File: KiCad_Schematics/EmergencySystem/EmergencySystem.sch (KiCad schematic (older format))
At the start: 20 parts, among them SW1 E-Stop_Switch, SW2 ON/OFF_Switch, SW3 E-StopButton02, SW4 E-StopButton01, SW5 ON/OFF_Switch, U1 Feather_32u4_RFM95, U10 Adafruit_2200mAh_LiPo, U11 e-Boot_BuckConverter, U2 T3_EmergencyLight_RED, U3 T3_EmergencyLight_BLUE, U4 T3_EmergencyLight_AMBER, U5 Adafruit_2200mAh_LiPo, U6 OLED_I2C_Display, U7 Elegoo_4RelayModule, U8 e-Boot_BuckConverter, U9 Feather_32u4_RFM95

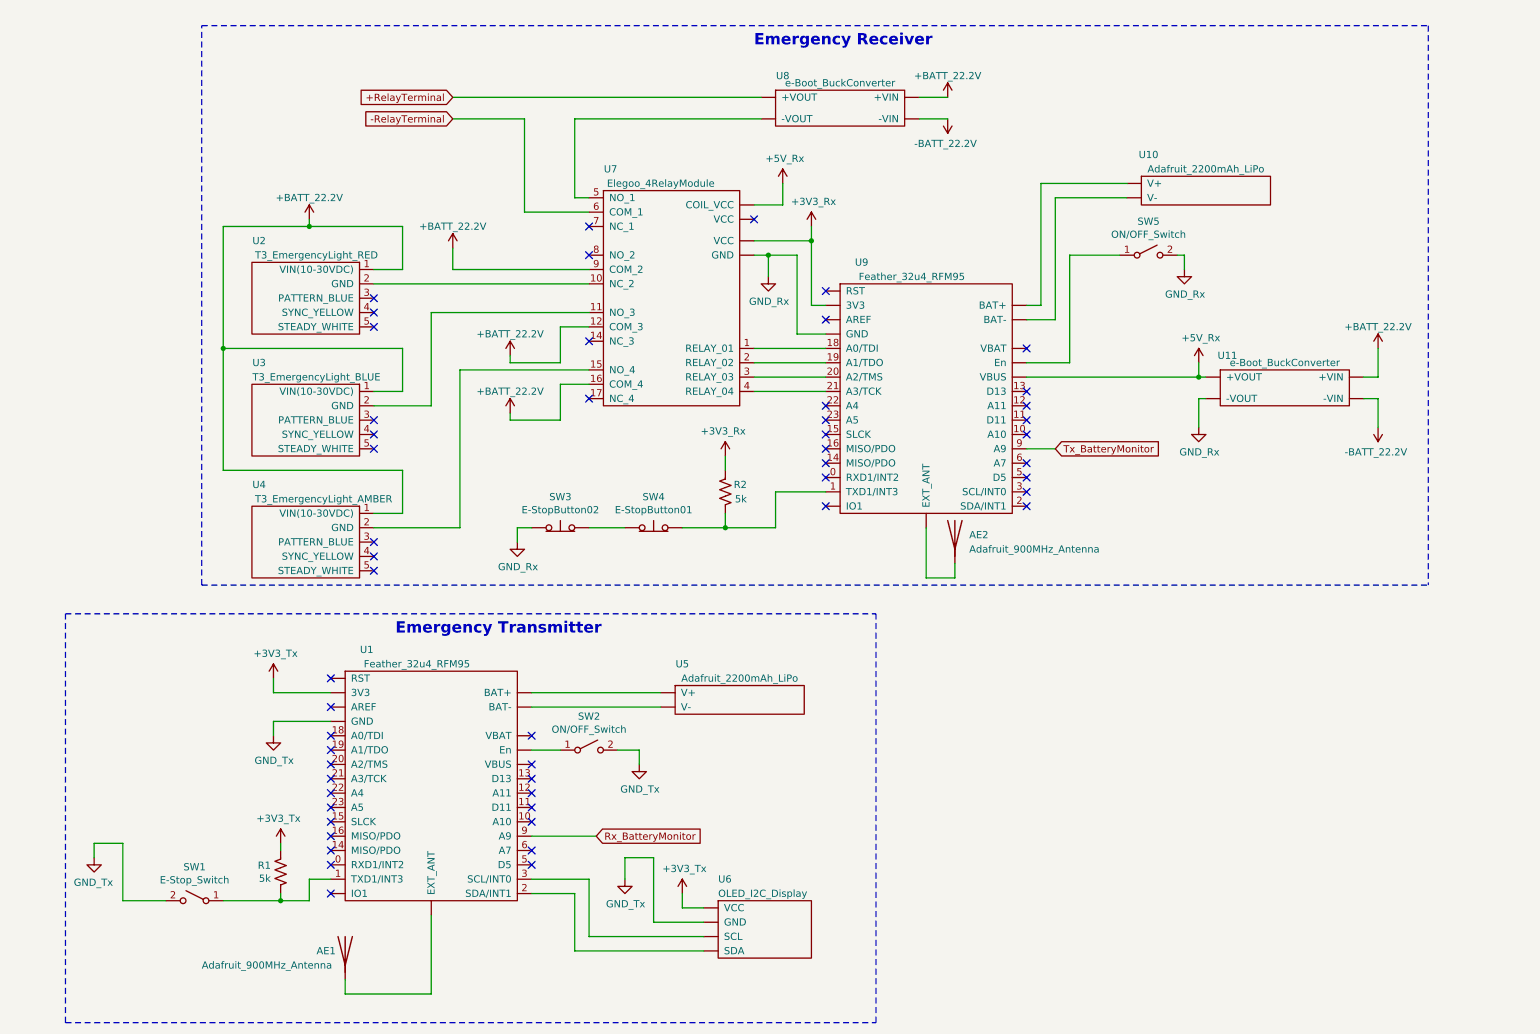
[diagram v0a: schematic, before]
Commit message: Updated the kicad schatic to include the logic-level shifter. Also modified the layout to indicate the emergency receiver components that are on the inside/outside of the boat
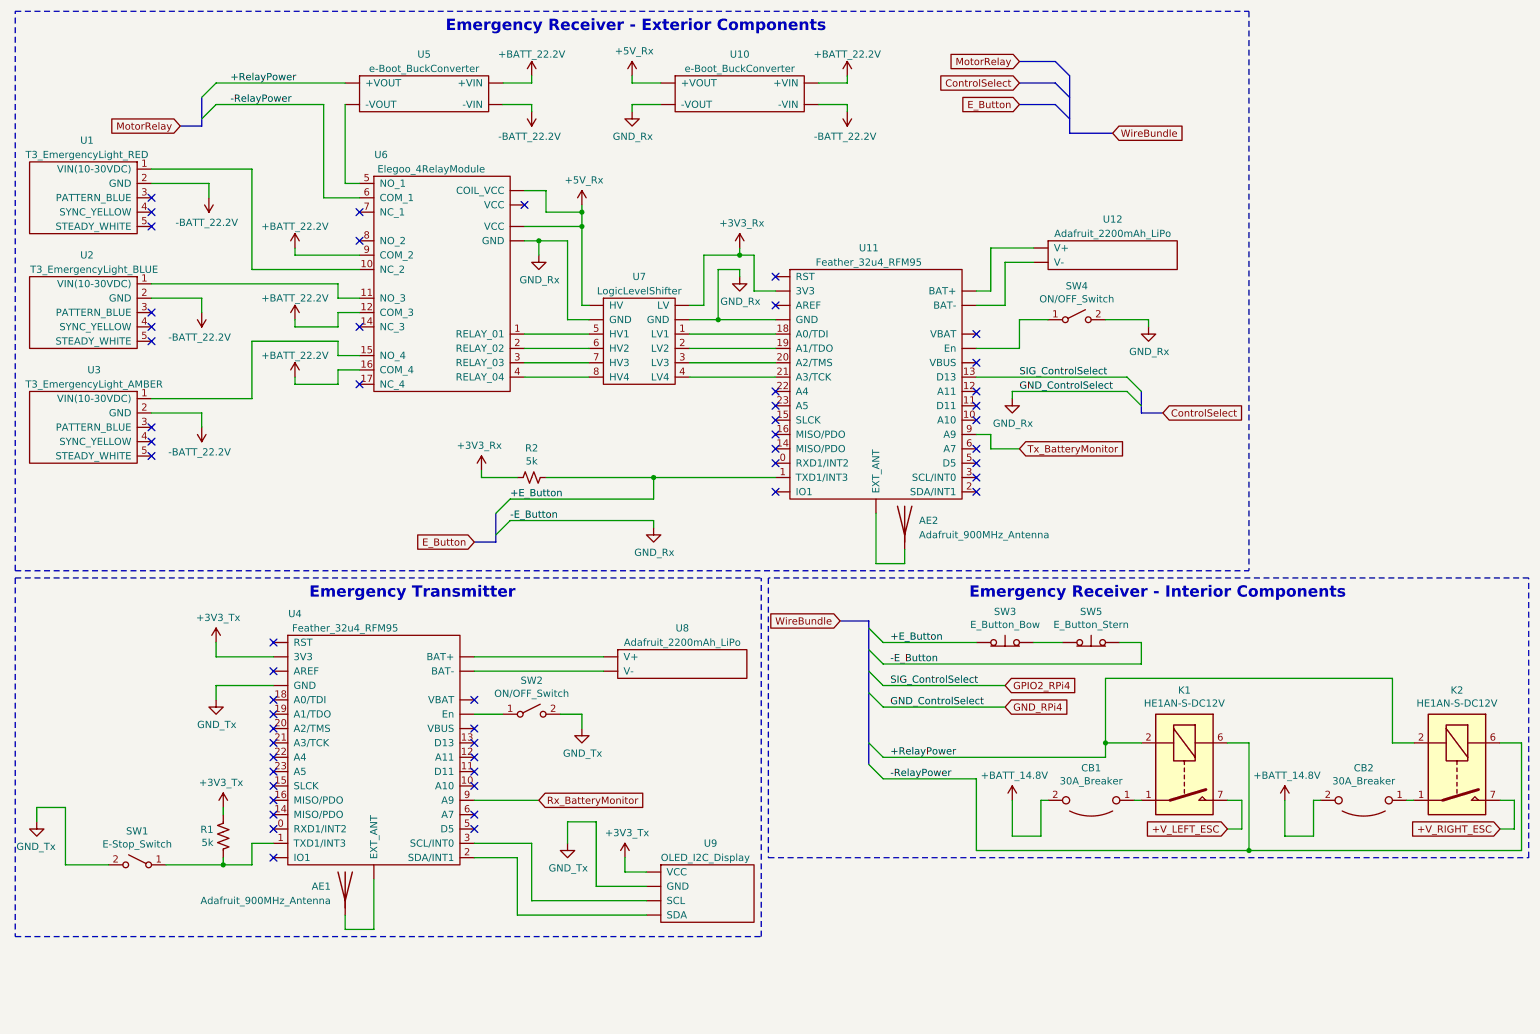
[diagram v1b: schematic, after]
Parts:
- removed R2: 5k, symbol Device:R_US
- added CB1, CB2: 30A_Breaker, symbol Device:CircuitBreaker_1P_US
- added K1, K2: HE1AN-S-DC12V, Relay_THT:Relay_StandexMeder_DIP_LowProfile, symbol Relay:DIPxx-1Axx-12x
- added R2: 5k, symbol Device:R_Small_US
- added U7: LogicLevelShifter, symbol RoboBoat_Parts:LogicLevelShifter
- SW3: value E-StopButton02 -> E_Button_Bow
- SW5: renamed from SW4; value E-StopButton01 -> E_Button_Stern
- renumbered SW5 to SW4, U2 to U1, U11 to U10, U9 to U11, U10 to U12, U3 to U2, U4 to U3, U1 to U4, U8 to U5, U7 to U6, U5 to U8, U6 to U9
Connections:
- net +3V3: now also R2.2, U7.~ (LV); no longer U6.~ (VCC)
- net +5V: now also U7.~ (LV); no longer U11.~ (EXT_ANT)
- net +BATT: now also U1.2 (GND), U2.2 (GND), U3.2 (GND), CB1.2, CB2.2; no longer U1.1 (VIN(10-30VDC)), U2.1 (VIN(10-30VDC)), U3.1 (VIN(10-30VDC))
- net GND: now also SW5.1 (A), U7.~ (LV); no longer SW3.1 (A)
- net +E_Button: now reaches U11.1 (TXD1/INT3)
- net +E_Button: now also SW3.1 (A), R2.1; no longer SW5.1 (A)
- net GPIO2_RPi4: now reaches U11.13 (D13)
- net at U11.18 (A0/TDI): now also U7.1 (LV1); no longer U6.1 (RELAY_01)
- net at U11.19 (A1/TDO): now also U7.2 (LV2); no longer U6.2 (RELAY_02)
- net at U11.20 (A2/TMS): now also U7.3 (LV3); no longer U6.3 (RELAY_03)
- net at U11.21 (A3/TCK): now also U7.4 (LV4); no longer U6.4 (RELAY_04)
- net at U6.10 (NC_2): now also U1.1 (VIN(10-30VDC)); no longer U1.2 (GND)
- net at U6.11 (NO_3): now also U2.1 (VIN(10-30VDC)); no longer U2.2 (GND)
- net at U6.15 (NO_4): now also U3.1 (VIN(10-30VDC)); no longer U3.2 (GND)
- net +RelayTerminal renamed +RelayPower
- net +RelayPower: now also K1.13, K1.2, K2.13, K2.2
- net -RelayTerminal renamed -RelayPower
- net -RelayPower: now also K1.6, K2.6
- new net: U11.~ (EXT_ANT), U12.~ (V-)
- new net: U6.1 (RELAY_01), U7.5 (HV1)
- new net: U6.2 (RELAY_02), U7.6 (HV2)
- new net: U6.3 (RELAY_03), U7.7 (HV3)
- new net: U6.4 (RELAY_04), U7.8 (HV4)
- new net: U4.~ (EXT_ANT), U8.~ (V-)
- new net: CB1.1, K1.1, K1.14
- new net: CB2.1, K2.1, K2.14
- new net +V_LEFT_ESC: K1.7, K1.8
- new net +V_RIGHT_ESC: K2.7, K2.8
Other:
- note added: "Emergency Receiver - Exterior Components"
- note added: "Emergency Receiver - Interior Components"
- note removed: "Emergency Receiver"
- moved on the sheet: AE2, R1, SW1, SW2, SW3, SW4, SW5, U1, U10, U11, U12, U2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

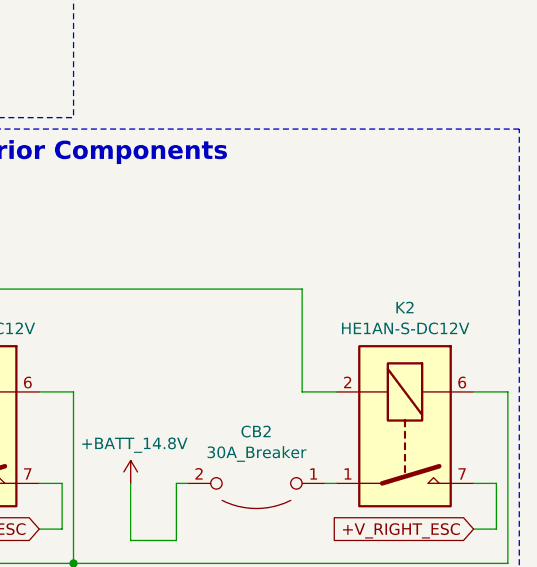
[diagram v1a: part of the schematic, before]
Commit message: Updated images and schematics
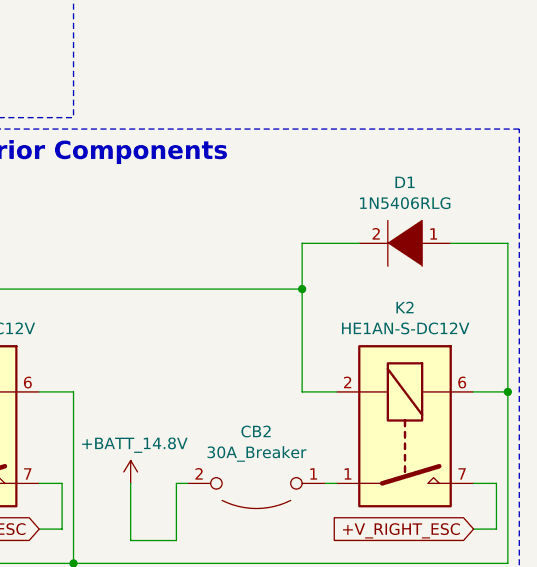
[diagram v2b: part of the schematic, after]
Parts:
- added D1: 1N5406RLG, symbol pspice:DIODE
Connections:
- net +RelayPower: now also D1.2 (A)
- net -RelayPower: now also D1.1 (K)
- new net: U11.~ (EXT_ANT), U12.~ (V-)
- new net: U4.~ (EXT_ANT), U8.~ (V-)
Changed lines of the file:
@@
 Title "Emergency Transmitter and Receiver"
 Date "2020-02-03"
-Rev "3"
+Rev "4"
 Comp "Temple University College of Engineering"
 Comment1 "Author: Byron Gaspard"
@@
 Wire Notes Line
 	5750 6400 11050 6400
+$Comp
+L pspice:DIODE D1
+U 1 1 5E983D34
+P 10550 4950
+F 0 "D1" H 10550 4685 50  0000 C CNN
+F 1 "1N5406RLG" H 10550 4776 50  0000 C CNN
+F 2 "" H 10550 4950 50  0001 C CNN
+F 3 "~" H 10550 4950 50  0001 C CNN
+	1    10550 4950
+	-1   0    0    1
+$EndComp
+Wire Wire Line
+	10350 4950 10100 4950
+Wire Wire Line
+	10100 4950 10100 5150
+Connection ~ 10100 5150
+Wire Wire Line
+	10750 4950 11000 4950
+Wire Wire Line
+	11000 4950 11000 5600
 Wire Bus Line
 	8350 3150 8350 3300
@@
 Wire Bus Line
 	6450 4750 6450 5750
+Connection ~ 11000 5600
 $EndSCHEMATC

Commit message: updated schematics
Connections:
- new net: U11.~ (EXT_ANT), U12.~ (V-)
- new net: U4.~ (EXT_ANT), U8.~ (V-)
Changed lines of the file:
@@
 Sheet 1 1
 Title "Emergency Transmitter and Receiver"
-Date "2020-02-03"
+Date "2020-04-23"
 Rev "4"
 Comp "Temple University College of Engineering"
@@
 Wire Wire Line
 	11000 4950 11000 5600
+Connection ~ 11000 5600
 Wire Bus Line
 	8350 3150 8350 3300
@@
 Wire Bus Line
 	6450 4750 6450 5750
-Connection ~ 11000 5600
 $EndSCHEMATC

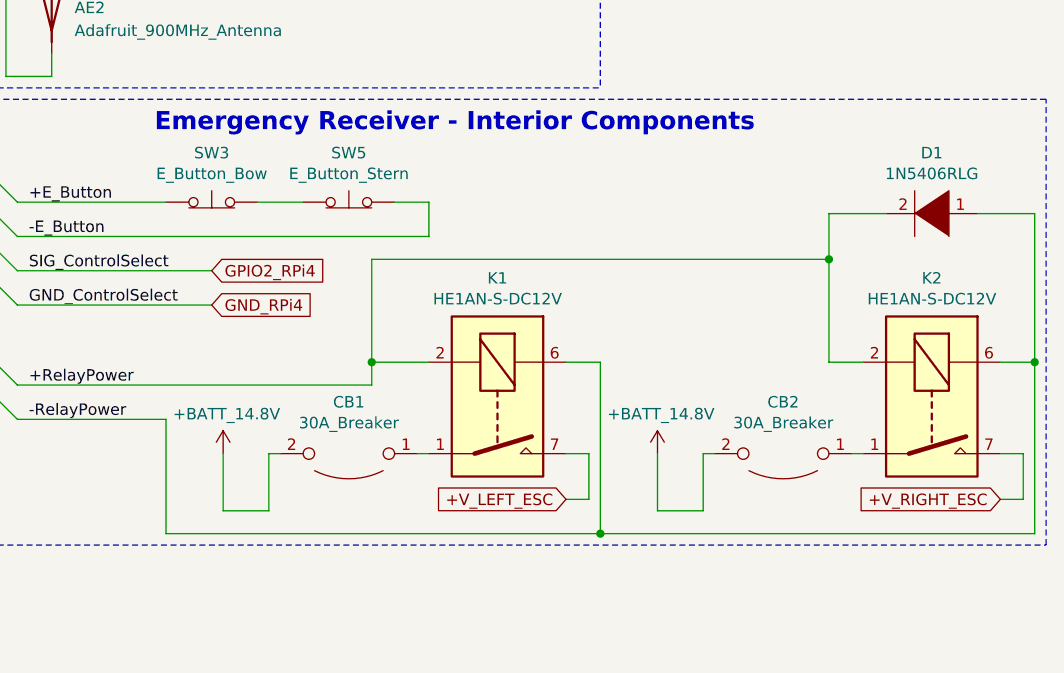
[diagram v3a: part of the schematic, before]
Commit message: Updates to images, schematics, and arduino code
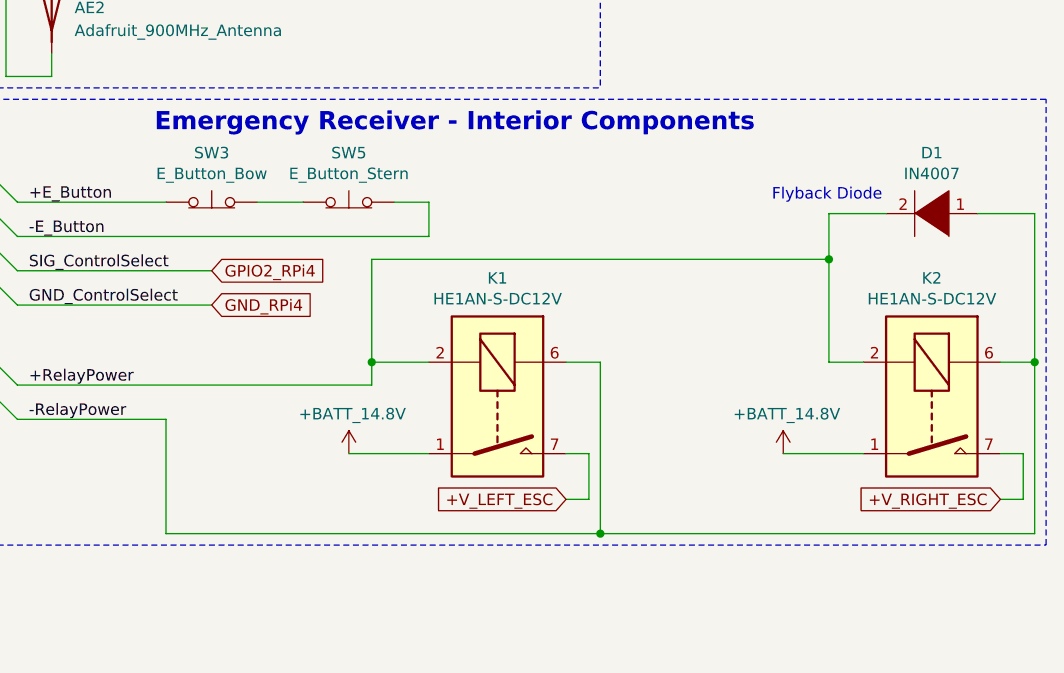
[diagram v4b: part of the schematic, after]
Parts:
- removed CB1, CB2: 30A_Breaker, symbol Device:CircuitBreaker_1P_US
- D1: value 1N5406RLG -> IN4007
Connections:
- net +BATT: now also K1.1, K1.14, K2.1, K2.14
- new net: U11.~ (EXT_ANT), U12.~ (V-)
- new net: U4.~ (EXT_ANT), U8.~ (V-)
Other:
- note added: "Flyback Diode"
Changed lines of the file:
@@
 Sheet 1 1
 Title "Emergency Transmitter and Receiver"
-Date "2020-04-23"
-Rev "4"
+Date "2020-04-30"
+Rev "5"
 Comp "Temple University College of Engineering"
 Comment1 "Author: Byron Gaspard"
@@
 L RoboBoat_PowerSymbols:+BATT_14.8V #PWR027
 U 1 1 5EDD33F6
-P 7450 6000
-F 0 "#PWR027" H 7450 5850 50  0001 C CNN
-F 1 "+BATT_14.8V" H 7465 6173 50  0000 C CNN
-F 2 "" H 7450 6000 50  0001 C CNN
-F 3 "" H 7450 6000 50  0001 C CNN
-	1    7450 6000
+P 8000 6000
+F 0 "#PWR027" H 8000 5850 50  0001 C CNN
+F 1 "+BATT_14.8V" H 8015 6173 50  0000 C CNN
+F 2 "" H 8000 6000 50  0001 C CNN
+F 3 "" H 8000 6000 50  0001 C CNN
+	1    8000 6000
 	1    0    0    -1
 $EndComp
@@
 Wire Notes Line
 	500  4400 9100 4400
-$Comp
-L Device:CircuitBreaker_1P_US CB1
-U 1 1 5E6B42EB
-P 8000 6000
-F 0 "CB1" V 7775 6000 50  0000 C CNN
-F 1 "30A_Breaker" V 7866 6000 50  0000 C CNN
-F 2 "" H 8000 6000 50  0001 C CNN
-F 3 "~" H 8000 6000 50  0001 C CNN
-	1    8000 6000
-	0    1    1    0
-$EndComp
-Wire Wire Line
-	7700 6000 7650 6000
-Wire Wire Line
-	7650 6000 7650 6250
-Wire Wire Line
-	7450 6000 7450 6250
-Wire Wire Line
-	7450 6250 7650 6250
-Wire Wire Line
-	8350 6000 8300 6000
 Wire Wire Line
 	10100 5150 10100 5600
@@
 Wire Wire Line
 	7200 5850 6550 5850
-$Comp
-L RoboBoat_PowerSymbols:+BATT_14.8V #PWR029
-U 1 1 5E80EB81
-P 9350 6000
-F 0 "#PWR029" H 9350 5850 50  0001 C CNN
-F 1 "+BATT_14.8V" H 9365 6173 50  0000 C CNN
-F 2 "" H 9350 6000 50  0001 C CNN
-F 3 "" H 9350 6000 50  0001 C CNN
-	1    9350 6000
-	1    0    0    -1
-$EndComp
-$Comp
-L Device:CircuitBreaker_1P_US CB2
-U 1 1 5E80EB87
-P 9900 6000
-F 0 "CB2" V 9675 6000 50  0000 C CNN
-F 1 "30A_Breaker" V 9766 6000 50  0000 C CNN
-F 2 "" H 9900 6000 50  0001 C CNN
-F 3 "~" H 9900 6000 50  0001 C CNN
-	1    9900 6000
-	0    1    1    0
-$EndComp
-Wire Wire Line
-	9600 6000 9550 6000
-Wire Wire Line
-	9550 6000 9550 6250
-Wire Wire Line
-	9350 6000 9350 6250
-Wire Wire Line
-	9350 6250 9550 6250
-Wire Wire Line
-	10250 6000 10200 6000
 Wire Wire Line
 	7200 6350 9100 6350
@@
 P 10550 4950
 F 0 "D1" H 10550 4685 50  0000 C CNN
-F 1 "1N5406RLG" H 10550 4776 50  0000 C CNN
+F 1 "IN4007" H 10550 4776 50  0000 C CNN
 F 2 "" H 10550 4950 50  0001 C CNN
 F 3 "~" H 10550 4950 50  0001 C CNN
@@
 	11000 4950 11000 5600
 Connection ~ 11000 5600
+Text Notes 9850 4900 0    50   ~ 0
+Flyback Diode
+Wire Wire Line
+	8000 6000 8350 6000
+$Comp
+L RoboBoat_PowerSymbols:+BATT_14.8V #PWR?
+U 1 1 5EAB3009
+P 9900 6000
+F 0 "#PWR?" H 9900 5850 50  0001 C CNN
+F 1 "+BATT_14.8V" H 9915 6173 50  0000 C CNN
+F 2 "" H 9900 6000 50  0001 C CNN
+F 3 "" H 9900 6000 50  0001 C CNN
+	1    9900 6000
+	1    0    0    -1
+$EndComp
+Wire Wire Line
+	9900 6000 10250 6000
 Wire Bus Line
 	8350 3150 8350 3300
